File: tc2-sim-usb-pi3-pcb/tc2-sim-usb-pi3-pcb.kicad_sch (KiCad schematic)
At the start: 5 parts, among them J11 Conn_01x08, J2 Conn_01x03

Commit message: Upgrade to KiCAD 10
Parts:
- U1: value ~ -> (none)
- renumbered C37 to C1, D4 to D1, J11 to J1

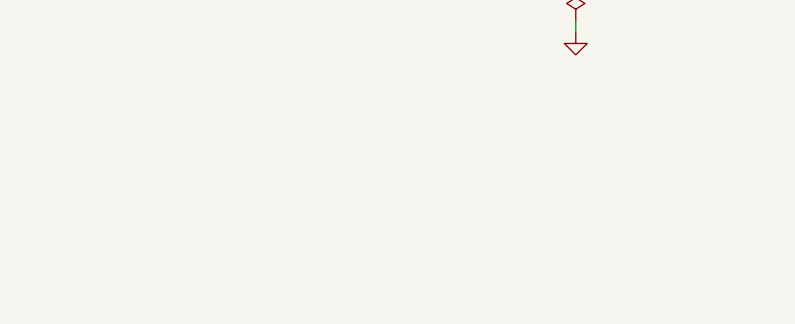
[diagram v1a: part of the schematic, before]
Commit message: Add JLPCPCB 2D barcode to PCBs
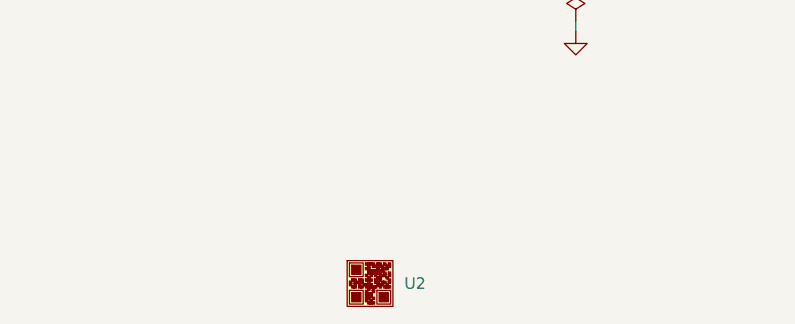
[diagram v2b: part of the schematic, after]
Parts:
- added U2: (no value), cacophony-library:JLCPCB_QR_8mm, symbol cacophony-library:JLCPCB_QR_CODE
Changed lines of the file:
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@@
+		)
+	)
+	(symbol
+		(lib_id "cacophony-library:JLCPCB_QR_CODE")
+		(at 87.63 138.43 0)
+		(unit 1)
+		(body_style 1)
+		(exclude_from_sim yes)
+		(in_bom no)
+		(on_board yes)
+		(in_pos_files no)
+		(dnp no)
+		(fields_autoplaced yes)
+		(property "Reference" "U2"
+			(at 91.44 138.4299 0)
+			(show_name no)
+			(do_not_autoplace no)
+			(effects
+				(font
+					(size 1.27 1.27)
+				)
+				(justify left)
+			)
+		)
+		(property "Value" ""
+			(at 87.63 138.43 0)
+			(show_name no)
+			(do_not_autoplace no)
+			(effects
+				(font
+					(size 1.27 1.27)
+				)
+			)
+		)
+		(property "Footprint" "cacophony-library:JLCPCB_QR_8mm"
+			(at 87.63 138.43 0)
+			(hide yes)
+			(show_name no)
+			(do_not_autoplace no)
+			(effects
+				(font
+					(size 1.27 1.27)
+				)
+			)
+		)
+		(property "Datasheet" ""
+			(at 87.63 138.43 0)
+			(hide yes)
+			(show_name no)
+			(do_not_autoplace no)
+			(effects
+				(font
+					(size 1.27 1.27)
+				)
+			)
+		)
+		(property "Description" ""
+			(at 87.63 138.43 0)
+			(hide yes)
+			(show_name no)
+			(do_not_autoplace no)
+			(effects
+				(font
+					(size 1.27 1.27)
+				)
+			)
+		)
+		(instances
+			(project "tc2-sim-usb-pi3-pcb"
+				(path "/d770f411-95fd-4fb5-bc90-145cf14a1a1d"
+					(reference "U2")
+					(unit 1)
+				)
+			)
 		)
 	)

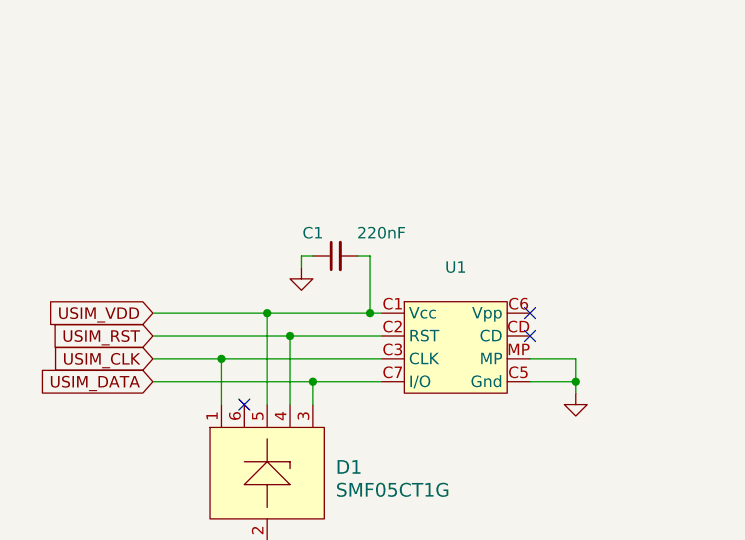
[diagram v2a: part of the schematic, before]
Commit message: Fix ERC errors
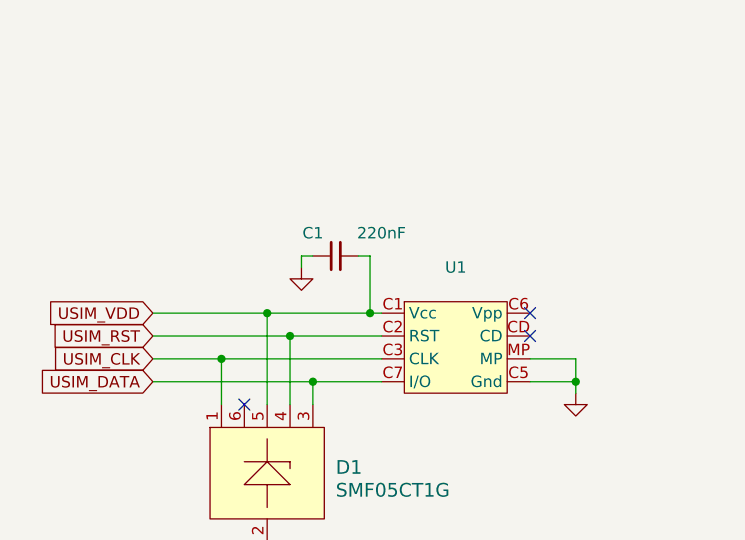
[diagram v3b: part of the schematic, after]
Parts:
- C1: LCSC C16772 -> (none); LCSC Part (none) -> C16772
- D1: LCSC C15879 -> (none); LCSC Part (none) -> C15879
- J1: now left out of the parts list
- J2: LCSC C491707 -> (none); LCSC Part (none) -> C491707
- U1: LCSC C2919617 -> (none); LCSC Part (none) -> C2919617
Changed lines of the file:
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@@
 			)
 		)
-		(property "LCSC" "C15879"
+		(property "LCSC Part" "C15879"
 			(at 76.2 90.17 0)
 			(hide yes)
@@
 		(body_style 1)
 		(exclude_from_sim no)
-		(in_bom yes)
+		(in_bom no)
 		(on_board yes)
-		(in_pos_files yes)
+		(in_pos_files no)
 		(dnp no)
 		(fields_autoplaced yes)
@@
 			)
 		)
-		(property "LCSC" "C491707"
+		(property "LCSC Part" "C491707"
 			(at 180.34 45.72 0)
 			(hide yes)
@@
 			)
 		)
-		(property "LCSC" "C16772"
+		(property "LCSC Part" "C16772"
 			(at 83.82 67.31 0)
 			(hide yes)
@@
 			)
 		)
-		(property "LCSC" "C2919617"
+		(property "LCSC Part" "C2919617"
 			(at 97.155 69.85 0)
 			(hide yes)
